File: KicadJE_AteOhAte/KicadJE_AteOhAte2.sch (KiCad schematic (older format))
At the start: 108 parts, among them J201 In_Accent, J202 In Gate, J203 Out Tom, P201 Doepfer_Power_10pin, Q201 MMBT2222A, Q202 MMBT2222A, Q203 MMBT2222A, Q204 MMBT2907A, Q205 MMBT2222A, Q206 MMBT2222A, SW201 Con/Tom, U201 TL072, U202 TL072, U203 TL072

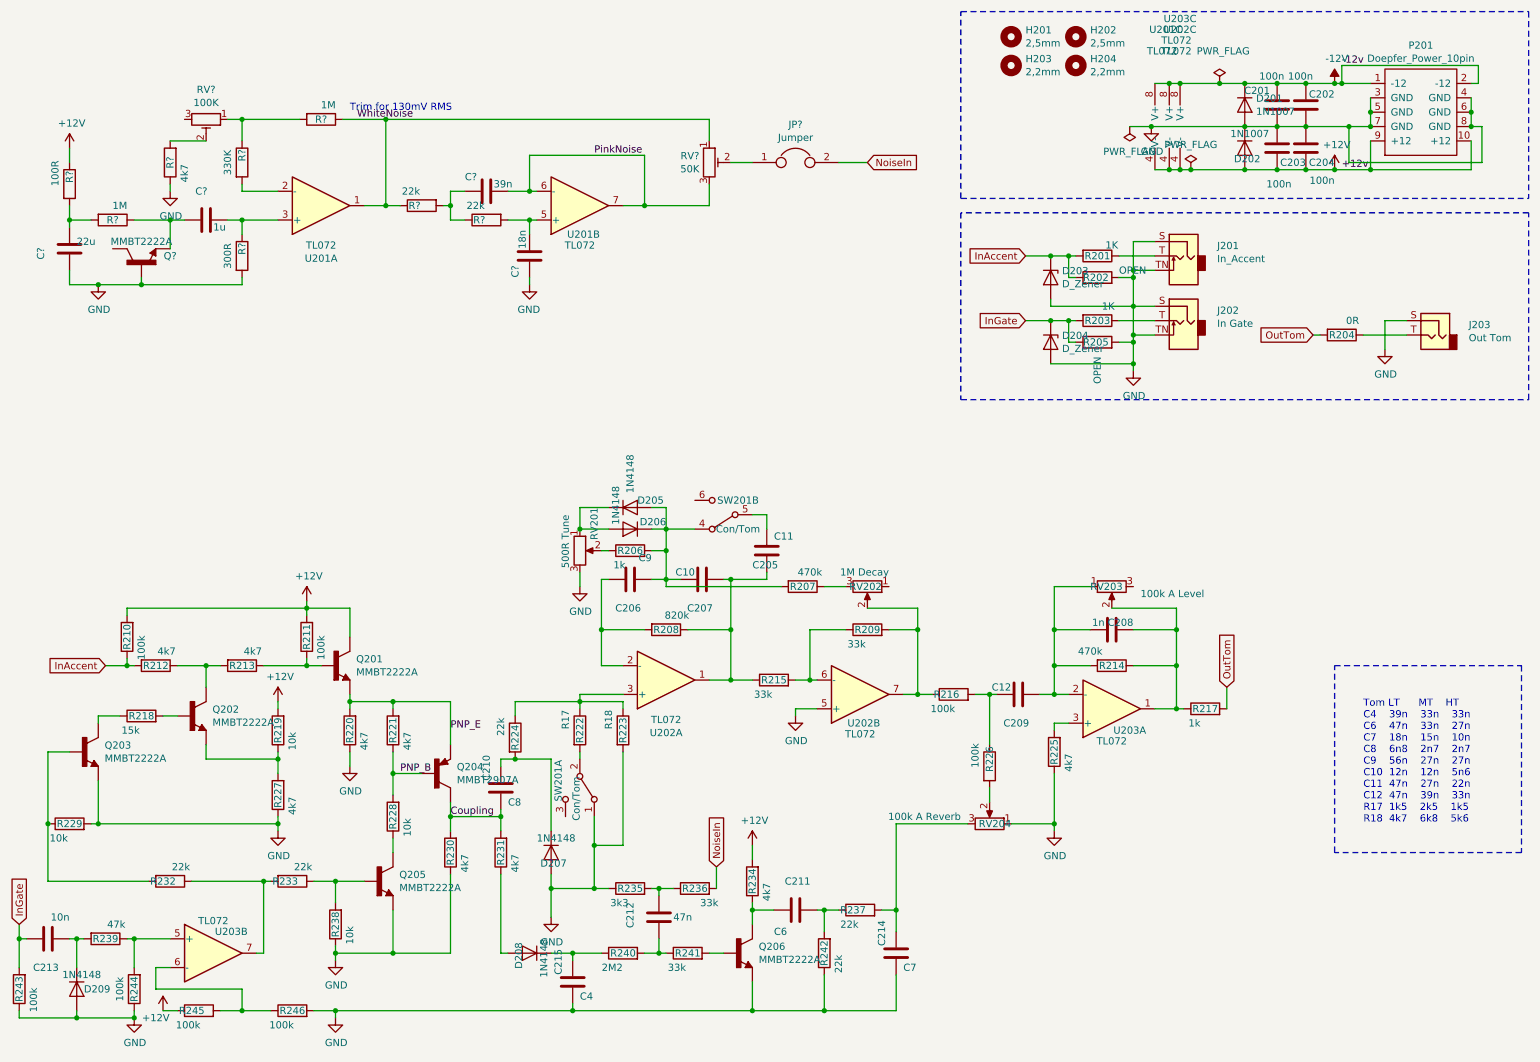
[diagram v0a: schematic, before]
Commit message: 2907 footprint and more
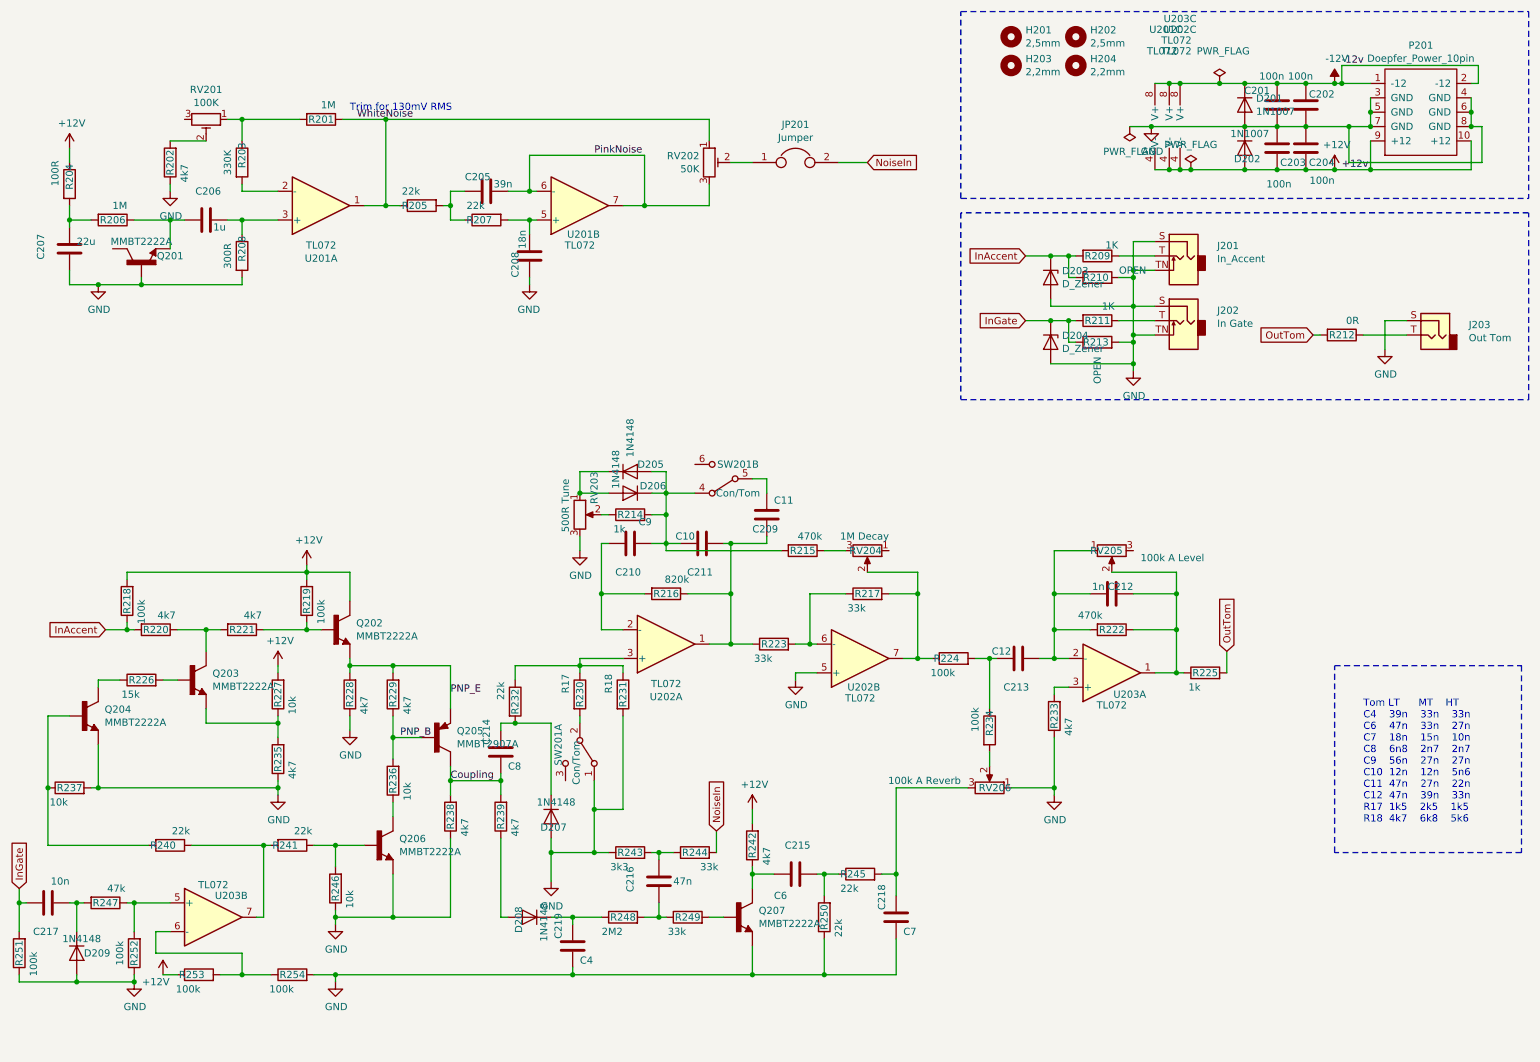
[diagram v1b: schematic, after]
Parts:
- gave numbers to parts that had none: 16
- renumbered C205 to C209, C206 to C210, C207 to C211, C208 to C212, C209 to C213, C210 to C214, C211 to C215, C212 to C216, C213 to C217, C214 to C218, C215 to C219, Q201 to Q202, Q202 to Q203, Q203 to Q204, Q204 to Q205, Q205 to Q206, Q206 to Q207, R201 to R209, R202 to R210, R203 to R211, R204 to R212, R205 to R213, R206 to R214, R207 to R215, R208 to R216, R209 to R217, R210 to R218, R211 to R219, R212 to R220, R213 to R221, R214 to R222, R215 to R223, R216 to R224, R217 to R225, R218 to R226, R219 to R227, R220 to R228, R221 to R229, R222 to R230, R223 to R231, R224 to R232, R225 to R233, R226 to R234, R227 to R235, R228 to R236, R229 to R237, R230 to R238, R231 to R239, R232 to R240, R233 to R241, R234 to R242, R235 to R243, R236 to R244, R237 to R245, R238 to R246, R239 to R247, R240 to R248, R241 to R249, R242 to R250, R243 to R251, R244 to R252, R245 to R253, R246 to R254, RV201 to RV203, RV202 to RV204, RV203 to RV205, RV204 to RV206
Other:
- moved on the sheet: C209, C210, C211, C212, C213, C214, C215, C216, C217, C218, C219, D205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

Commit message: Test points for adj
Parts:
- added TP201: WhiteNoise, TestPoint:TestPoint_Pad_1.5x1.5mm, symbol Connector:TestPoint
- added TP202: GND, TestPoint:TestPoint_THTPad_2.0x2.0mm_Drill1.0mm, symbol Connector:TestPoint
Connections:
- net GND: now also TP202.1
- net WhiteNoise: now also TP201.1
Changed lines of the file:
@@
 	2200 2050 2100 2050
 Wire Wire Line
-	1500 2500 2200 2500
+	1500 2500 1850 2500
 Wire Wire Line
 	2200 2500 2200 2450
@@
 $EndComp
 Wire Wire Line
-	3200 1350 5450 1350
+	3200 1350 3900 1350
 Wire Wire Line
 	5450 1350 5450 1500
@@
 Text Label 3650 5950 0    50   ~ 0
 Coupling
+$Comp
+L Connector:TestPoint TP201
+U 1 1 5F5477D7
+P 3900 1350
+F 0 "TP201" H 3958 1468 50  0000 L CNN
+F 1 "WhiteNoise" H 3958 1377 50  0000 L CNN
+F 2 "TestPoint:TestPoint_Pad_1.5x1.5mm" H 4100 1350 50  0001 C CNN
+F 3 "~" H 4100 1350 50  0001 C CNN
+	1    3900 1350
+	1    0    0    -1
+$EndComp
+Connection ~ 3900 1350
+Wire Wire Line
+	3900 1350 5450 1350
+$Comp
+L Connector:TestPoint TP202
+U 1 1 5F552749
+P 1850 2500
+F 0 "TP202" H 1908 2618 50  0000 L CNN
+F 1 "GND" H 1908 2527 50  0000 L CNN
+F 2 "TestPoint:TestPoint_THTPad_2.0x2.0mm_Drill1.0mm" H 2050 2500 50  0001 C CNN
+F 3 "~" H 2050 2500 50  0001 C CNN
+	1    1850 2500
+	1    0    0    -1
+$EndComp
+Connection ~ 1850 2500
+Wire Wire Line
+	1850 2500 2200 2500
 $EndSCHEMATC

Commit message: pcb
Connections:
- net at C210.2, C211.1, D205.2 (A)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: now also SW201.6 (C); no longer SW201.4 (A)
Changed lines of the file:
@@
 F 3 "~" H 5550 3850 50  0001 C CNN
 	2    5550 3850
-	-1   0    0    1
+	-1   0    0    -1
 $EndComp
 $Comp

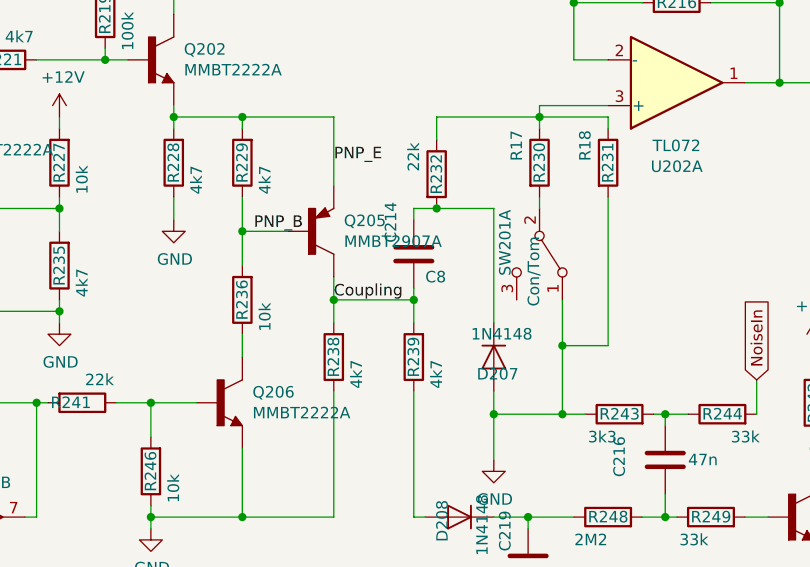
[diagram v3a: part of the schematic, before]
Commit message: PCB and Testpoint to coupling
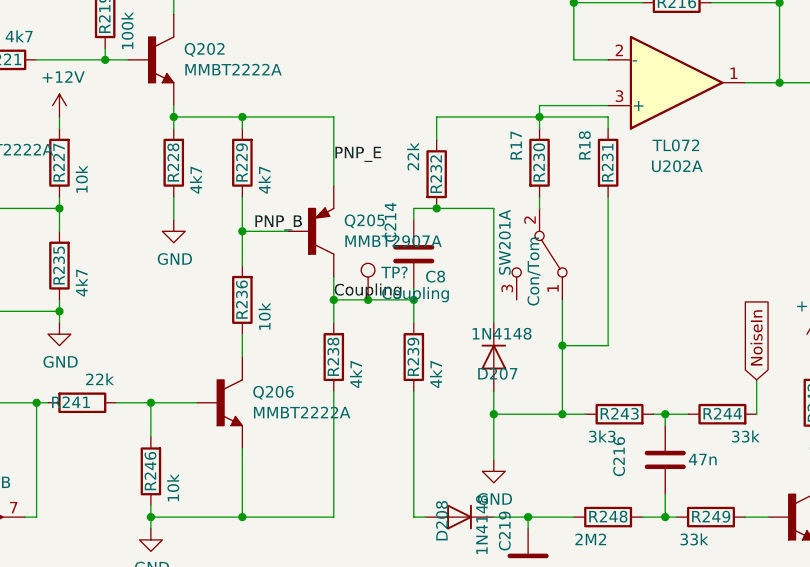
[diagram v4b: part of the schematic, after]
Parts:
- added TP?: Coupling, TestPoint:TestPoint_Pad_1.5x1.5mm, symbol Connector:TestPoint
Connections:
- net Coupling: now also TP?.1
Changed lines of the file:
@@
 $EndComp
 Wire Wire Line
-	3650 5950 4000 5950
+	3650 5950 3800 5950
 Connection ~ 3650 5950
 Wire Wire Line
@@
 Wire Wire Line
 	1850 2500 2200 2500
+$Comp
+L Connector:TestPoint TP?
+U 1 1 5DA7BFEF
+P 3800 5950
+F 0 "TP?" H 3858 6068 50  0000 L CNN
+F 1 "Coupling" H 3858 5977 50  0000 L CNN
+F 2 "TestPoint:TestPoint_Pad_1.5x1.5mm" H 4000 5950 50  0001 C CNN
+F 3 "~" H 4000 5950 50  0001 C CNN
+	1    3800 5950
+	1    0    0    -1
+$EndComp
+Connection ~ 3800 5950
+Wire Wire Line
+	3800 5950 4000 5950
 $EndSCHEMATC

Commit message: Sch
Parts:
- gave numbers to parts that had none: 1
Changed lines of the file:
@@
 	1850 2500 2200 2500
 $Comp
-L Connector:TestPoint TP?
+L Connector:TestPoint TP203
 U 1 1 5DA7BFEF
 P 3800 5950
-F 0 "TP?" H 3858 6068 50  0000 L CNN
+F 0 "TP203" H 3858 6068 50  0000 L CNN
 F 1 "Coupling" H 3858 5977 50  0000 L CNN
 F 2 "TestPoint:TestPoint_Pad_1.5x1.5mm" H 4000 5950 50  0001 C CNN

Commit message: sch RIAA
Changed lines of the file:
@@
-$EndComp
-$Comp
-L power:PWR_FLAG #FLG0202
-U 1 1 5C3F858C
-P 8375 1400
-F 0 "#FLG0202" H 8375 1475 50  0001 C CNN
-F 1 "PWR_FLAG" H 8375 1574 50  0000 C CNN
-F 2 "" H 8375 1400 50  0001 C CNN
-F 3 "~" H 8375 1400 50  0001 C CNN
-	1    8375 1400
-	-1   0    0    1
 $EndComp
 $Comp
@@
 Wire Wire Line
 	9850 1100 10050 1100
-$Comp
-L power:PWR_FLAG #FLG0201
-U 1 1 5C8AF822
-P 9000 1100
-F 0 "#FLG0201" H 9000 1175 50  0001 C CNN
-F 1 "PWR_FLAG" H 9025 1325 50  0000 C CNN
-F 2 "" H 9000 1100 50  0001 C CNN
-F 3 "~" H 9000 1100 50  0001 C CNN
-	1    9000 1100
-	1    0    0    -1
-$EndComp
-$Comp
-L power:PWR_FLAG #FLG0203
-U 1 1 5C8AF949
-P 8800 1700
-F 0 "#FLG0203" H 8800 1775 50  0001 C CNN
-F 1 "PWR_FLAG" H 8800 1874 50  0000 C CNN
-F 2 "" H 8800 1700 50  0001 C CNN
-F 3 "~" H 8800 1700 50  0001 C CNN
-	1    8800 1700
-	1    0    0    -1
-$EndComp
 Wire Notes Line
 	11150 600  11150 1900
@@
 	8650 1700 8725 1700
 Connection ~ 8725 1700
-Wire Wire Line
-	8725 1700 8800 1700
-Connection ~ 8800 1700
 Connection ~ 9175 1700
 Wire Wire Line
@@
 	8650 1100 8725 1100
 Connection ~ 8725 1100
-Wire Wire Line
-	8725 1100 9000 1100
-Connection ~ 9000 1100
-Wire Wire Line
-	9000 1100 9175 1100
 Connection ~ 9175 1100
 Wire Wire Line
@@
 Wire Wire Line
 	9600 1100 9800 1100
-Connection ~ 8525 1400
-Wire Wire Line
-	8375 1400 8525 1400
 Text Label 9850 975  0    50   ~ 0
 -12v
@@
 Wire Wire Line
 	8525 1400 9175 1400
-Wire Wire Line
-	8800 1700 9175 1700
 $Comp
 L power:-12V #PWR0201
@@
 Wire Wire Line
 	3800 5950 4000 5950
+Wire Wire Line
+	8725 1700 9175 1700
+Wire Wire Line
+	8725 1100 9175 1100
 $EndSCHEMATC

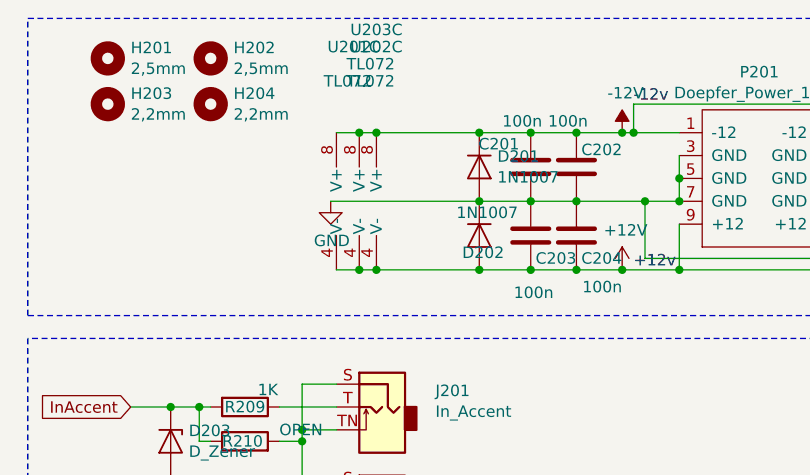
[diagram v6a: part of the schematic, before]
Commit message: Label upd and Added 2x caps to pwr
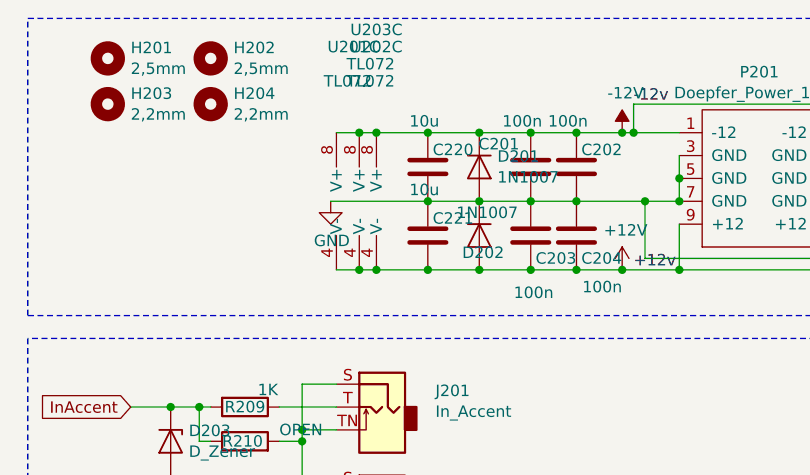
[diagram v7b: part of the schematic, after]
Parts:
- added C220, C221: 10u, Capacitor_SMD:C_1206_3216Metric_Pad1.42x1.75mm_HandSolder, symbol Device:C
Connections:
- net +12V: now also C221.1
- net -12V: now also C220.2
- net GND: now also C220.1, C221.2
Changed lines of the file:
@@
 	9800 1700 10050 1700
 Wire Wire Line
-	8525 1400 9175 1400
+	8525 1400 8950 1400
 $Comp
 L power:-12V #PWR0201
@@
 	3800 5950 4000 5950
 Wire Wire Line
-	8725 1700 9175 1700
-Wire Wire Line
-	8725 1100 9175 1100
+	8725 1700 8950 1700
+Wire Wire Line
+	8725 1100 8950 1100
+$Comp
+L Device:C C220
+U 1 1 5E7764B8
+P 8950 1250
+F 0 "C220" H 8750 1175 50  0000 L CNN
+F 1 "10u" H 8900 1050 50  0000 L CNN
+F 2 "Capacitor_SMD:C_1206_3216Metric_Pad1.42x1.75mm_HandSolder" H 8988 1100 50  0001 C CNN
+F 3 "~" H 8950 1250 50  0001 C CNN
+	1    8950 1250
+	-1   0    0    1
+$EndComp
+Connection ~ 8950 1400
+Wire Wire Line
+	8950 1400 9175 1400
+Connection ~ 8950 1100
+Wire Wire Line
+	8950 1100 9175 1100
+$Comp
+L Device:C C221
+U 1 1 5E776A40
+P 8950 1550
+F 0 "C221" H 8750 1475 50  0000 L CNN
+F 1 "10u" H 8900 1350 50  0000 L CNN
+F 2 "Capacitor_SMD:C_1206_3216Metric_Pad1.42x1.75mm_HandSolder" H 8988 1400 50  0001 C CNN
+F 3 "~" H 8950 1550 50  0001 C CNN
+	1    8950 1550
+	-1   0    0    1
+$EndComp
+Connection ~ 8950 1700
+Wire Wire Line
+	8950 1700 9175 1700
 $EndSCHEMATC
